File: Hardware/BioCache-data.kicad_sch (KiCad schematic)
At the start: 8 parts, among them U1 61C1024, U2 61C1024, U3 61C1024, U4 61C1024, U5 61C1024, U6 61C1024, U7 61C1024, U8 61C1024

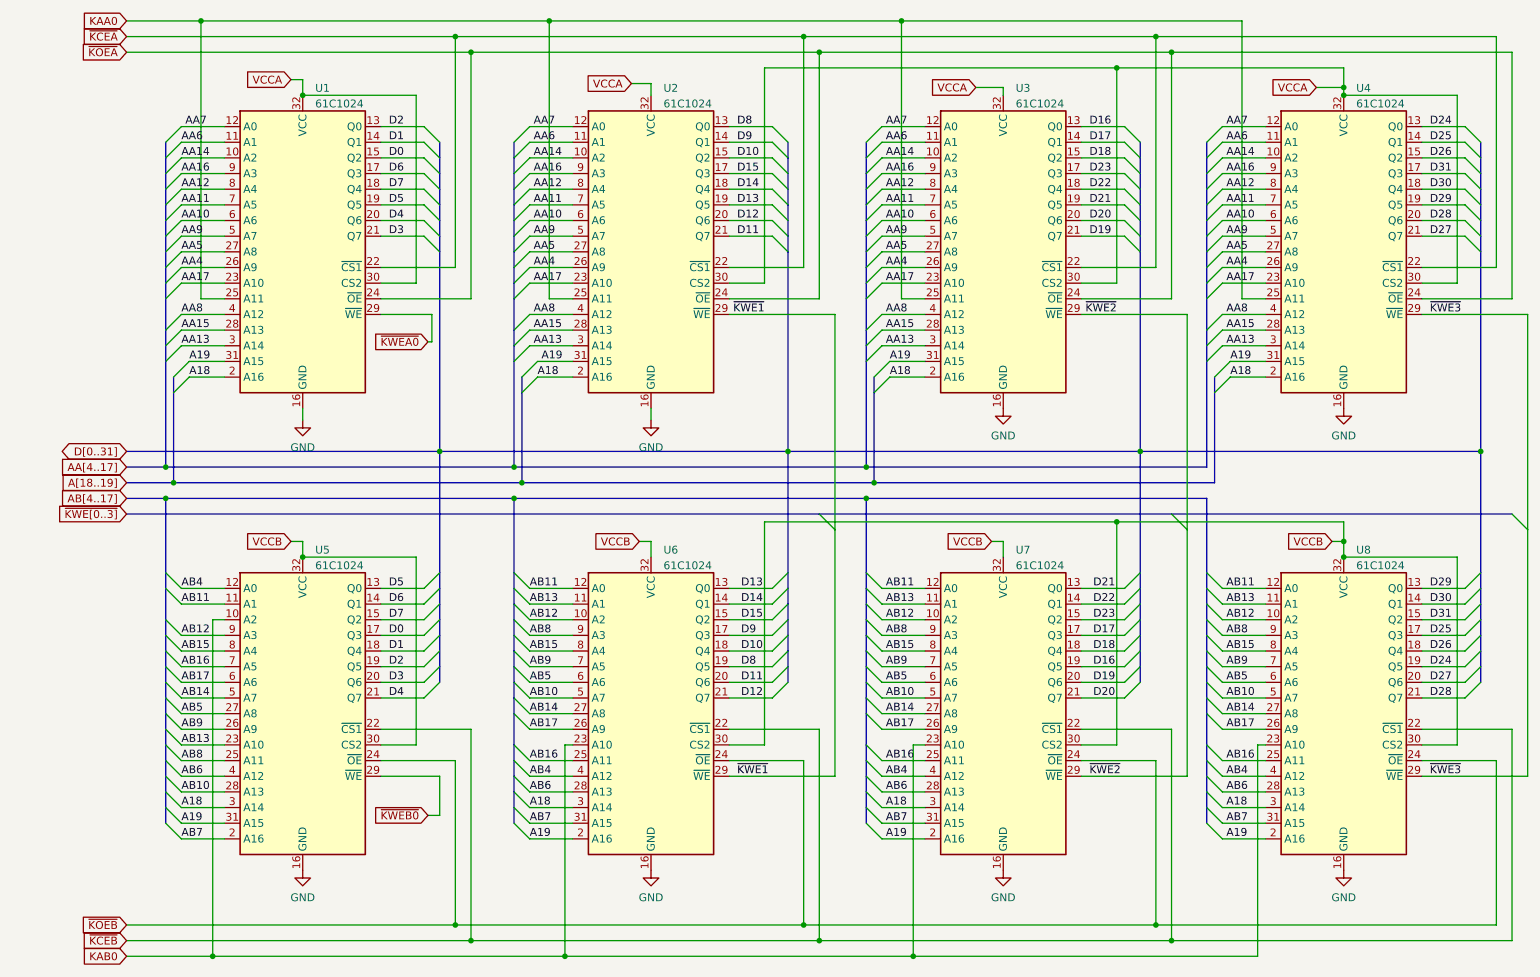
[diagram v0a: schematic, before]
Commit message: Upgrade to KiCad 9, clean-up schematics, set up KiBot
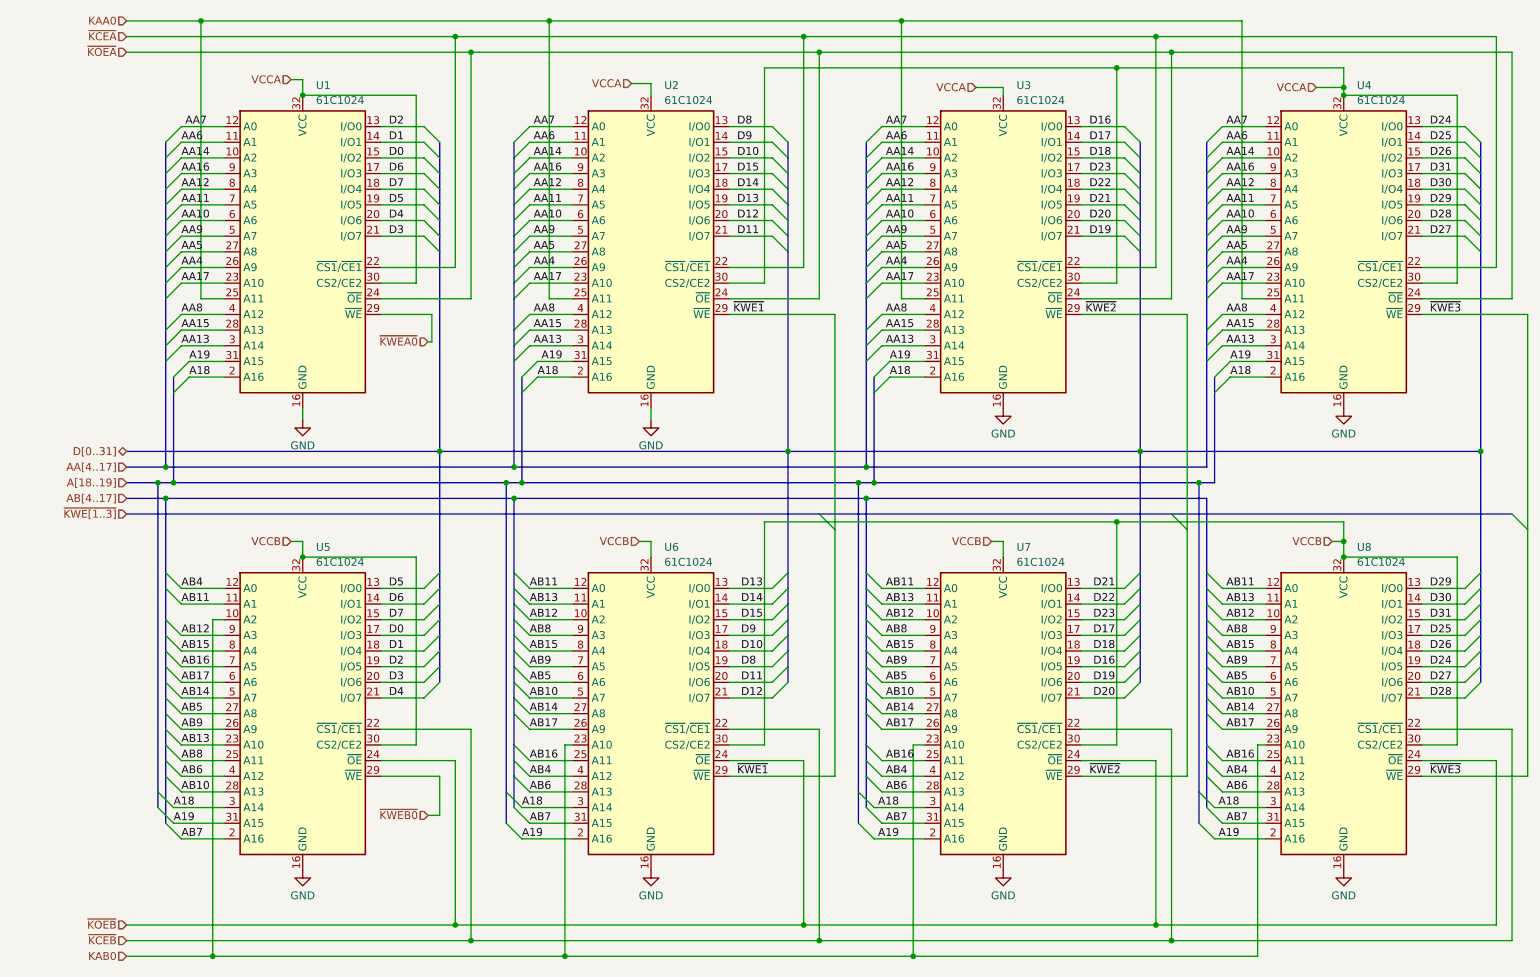
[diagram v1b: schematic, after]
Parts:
- U1, U2, U3, U4, U5, U6, U7, U8: symbol Memory_RAM:628128_DIP32_SSOP32 -> SOJmem:IS6xC1024AL-xxJ
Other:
- title: (none) -> Biostar MB-84xx-UUD 1MB cache data RAM

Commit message: Remove custom definition of SOJ32 memory chip
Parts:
- U1, U2, U3, U4, U5, U6, U7, U8: footprint Package_SOJ:SOJ-32_7.58x20.955mm_P1.27mm -> Package_SO:SOJ-32_7.62x20.955mm_P1.27mm; symbol SOJmem:IS6xC1024AL-xxJ -> Memory_RAM:IS6xC1024AL-xxJ
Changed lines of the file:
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@@
 	)
 	(symbol
-		(lib_id "SOJmem:IS6xC1024AL-xxJ")
+		(lib_id "Memory_RAM:IS6xC1024AL-xxJ")
 		(at 224.155 52.07 0)
 		(unit 1)
@@
 			)
 		)
-		(property "Footprint" "Package_SOJ:SOJ-32_7.58x20.955mm_P1.27mm"
+		(property "Footprint" "Package_SO:SOJ-32_7.62x20.955mm_P1.27mm"
 			(at 224.155 52.07 0)
 			(effects
@@
 	)
 	(symbol
-		(lib_id "SOJmem:IS6xC1024AL-xxJ")
+		(lib_id "Memory_RAM:IS6xC1024AL-xxJ")
 		(at 55.245 52.07 0)
 		(unit 1)
@@
 			)
 		)
-		(property "Footprint" "Package_SOJ:SOJ-32_7.58x20.955mm_P1.27mm"
+		(property "Footprint" "Package_SO:SOJ-32_7.62x20.955mm_P1.27mm"
 			(at 55.245 52.07 0)
 			(effects
@@
 	)
 	(symbol
-		(lib_id "SOJmem:IS6xC1024AL-xxJ")
+		(lib_id "Memory_RAM:IS6xC1024AL-xxJ")
 		(at 111.76 127 0)
 		(unit 1)
@@
 			)
 		)
-		(property "Footprint" "Package_SOJ:SOJ-32_7.58x20.955mm_P1.27mm"
+		(property "Footprint" "Package_SO:SOJ-32_7.62x20.955mm_P1.27mm"
 			(at 111.76 127 0)
 			(effects
@@
 	)
 	(symbol
-		(lib_id "SOJmem:IS6xC1024AL-xxJ")
+		(lib_id "Memory_RAM:IS6xC1024AL-xxJ")
 		(at 111.76 52.07 0)
 		(unit 1)
@@
 			)
 		)
-		(property "Footprint" "Package_SOJ:SOJ-32_7.58x20.955mm_P1.27mm"
+		(property "Footprint" "Package_SO:SOJ-32_7.62x20.955mm_P1.27mm"
 			(at 111.76 52.07 0)
 			(effects
@@
 	)
 	(symbol
-		(lib_id "SOJmem:IS6xC1024AL-xxJ")
+		(lib_id "Memory_RAM:IS6xC1024AL-xxJ")
 		(at 168.91 52.07 0)
 		(unit 1)
@@
 			)
 		)
-		(property "Footprint" "Package_SOJ:SOJ-32_7.58x20.955mm_P1.27mm"
+		(property "Footprint" "Package_SO:SOJ-32_7.62x20.955mm_P1.27mm"
 			(at 168.91 52.07 0)
 			(effects
@@
 	)
 	(symbol
-		(lib_id "SOJmem:IS6xC1024AL-xxJ")
+		(lib_id "Memory_RAM:IS6xC1024AL-xxJ")
 		(at 168.91 127 0)
 		(unit 1)
@@
 			)
 		)
-		(property "Footprint" "Package_SOJ:SOJ-32_7.58x20.955mm_P1.27mm"
+		(property "Footprint" "Package_SO:SOJ-32_7.62x20.955mm_P1.27mm"
 			(at 168.91 127 0)
 			(effects
@@
 	)
 	(symbol
-		(lib_id "SOJmem:IS6xC1024AL-xxJ")
+		(lib_id "Memory_RAM:IS6xC1024AL-xxJ")
 		(at 224.155 127 0)
 		(unit 1)
@@
 			)
 		)
-		(property "Footprint" "Package_SOJ:SOJ-32_7.58x20.955mm_P1.27mm"
+		(property "Footprint" "Package_SO:SOJ-32_7.62x20.955mm_P1.27mm"
 			(at 224.155 127 0)
 			(effects
@@
 	)
 	(symbol
-		(lib_id "SOJmem:IS6xC1024AL-xxJ")
+		(lib_id "Memory_RAM:IS6xC1024AL-xxJ")
 		(at 55.245 127 0)
 		(unit 1)
@@
 			)
 		)
-		(property "Footprint" "Package_SOJ:SOJ-32_7.58x20.955mm_P1.27mm"
+		(property "Footprint" "Package_SO:SOJ-32_7.62x20.955mm_P1.27mm"
 			(at 55.245 127 0)
 			(effects
